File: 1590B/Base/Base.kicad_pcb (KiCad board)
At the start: 2 copper layers, 54 x 106 mm, 44 parts, among them J101 Barrel_Jack_Switch, J102 AudioJack3_SwitchTR, J103 AudioJack3_SwitchTR, J201 Conn_02x04_Odd_Even, Q101 PMV250, Q102 BC846, Q103 BC846, Q201 LS844, Q301 DMC3071LVT, Q302 DMC3071LVT, SW101 SW_Push_SPDT, U101 Daisy Seed

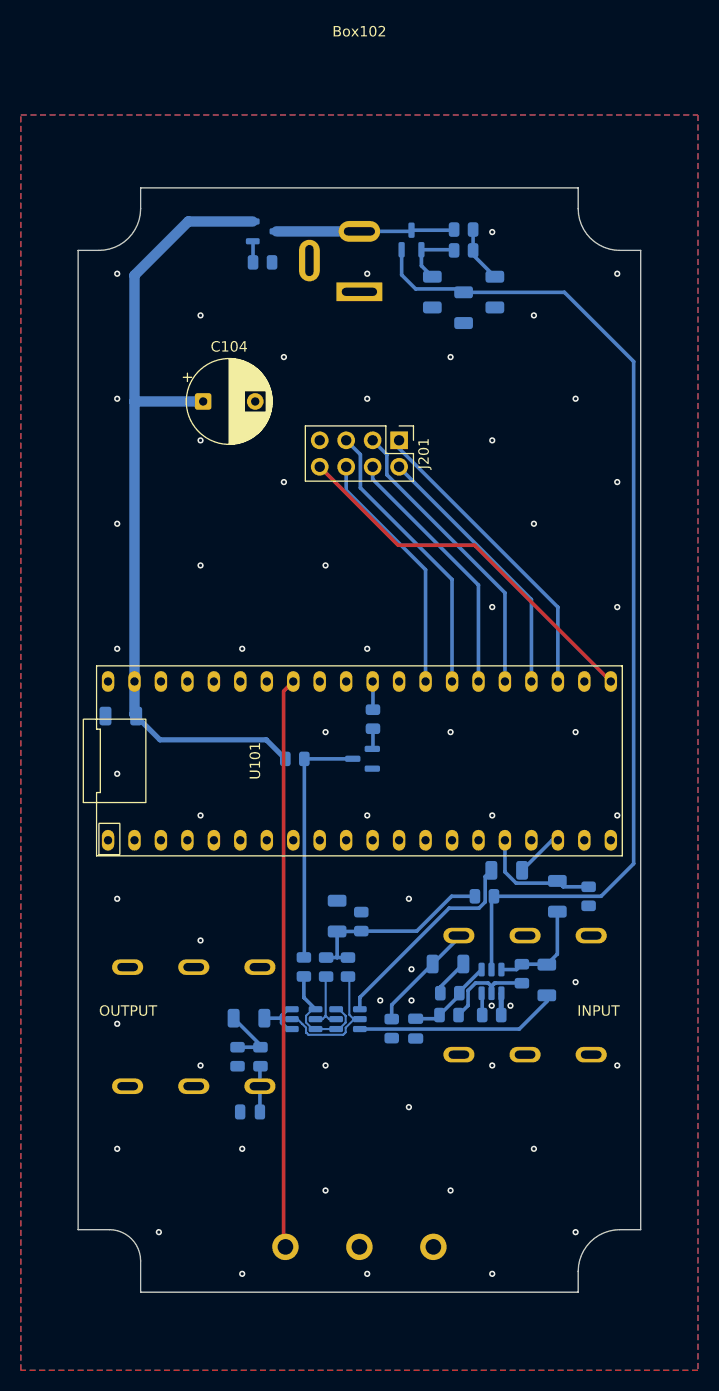
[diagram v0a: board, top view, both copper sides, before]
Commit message: Update 1590B board for sanity
I had entirely forgotten the activity LED, which was really annoying
when testing.

Also, while the transistor follower / capacitor multiplier on the analog
power supply was interesting for some low frequency power supply ripple
removal in simulation, it doesn't actually make any sense with any
modern power supply, so just do a regular RC filter for high
frequencies, which is what actually matters.

Together with the fixed potentiometer board, I think this should now
work nicely.

Famous last words.

Signed-off-by: Linus Torvalds <torvalds@linux-foundation.org>
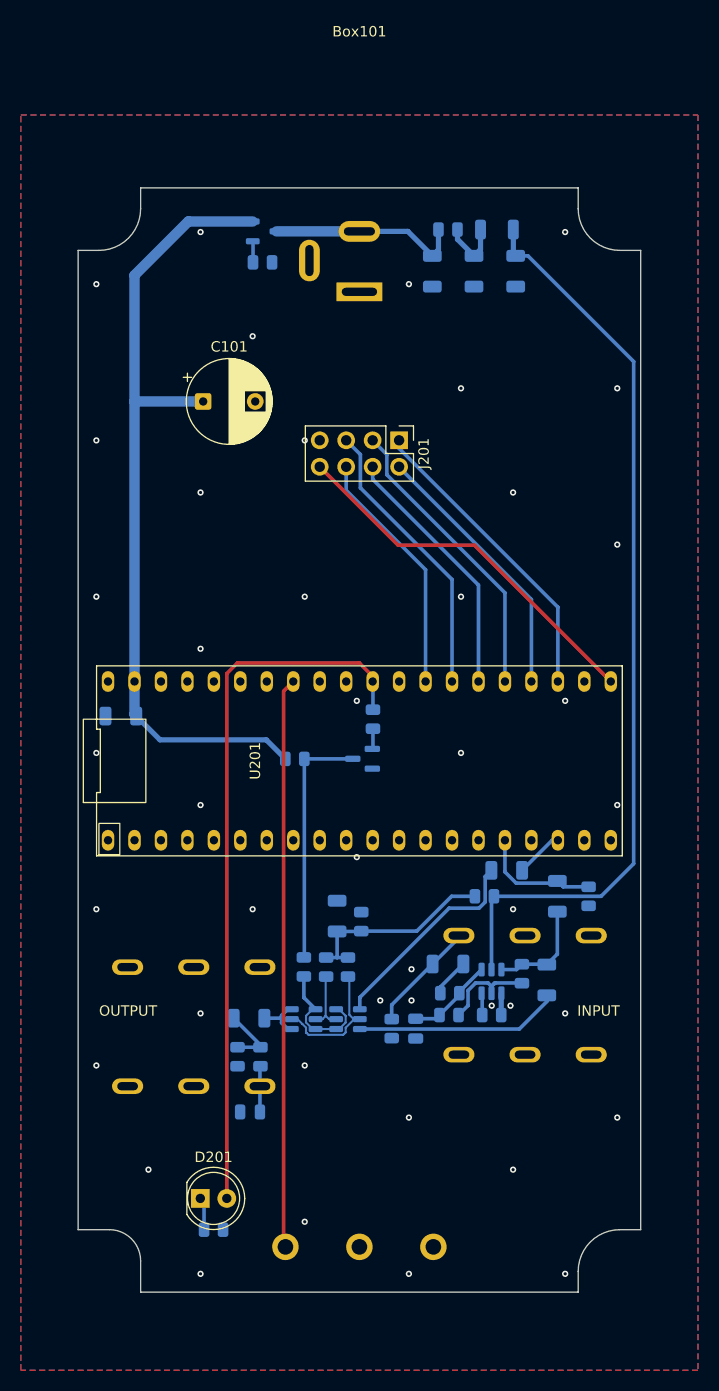
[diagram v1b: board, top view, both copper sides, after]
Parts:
- removed the C101 at (113.0, 57.0)
- removed Q102: BC846, Package_TO_SOT_SMD:SOT-23
- removed R106, R107: 2k2, Resistor_SMD:R_0805_2012Metric
- added C104: 1uF, Capacitor_SMD:C_1206_3216Metric, B.Cu at (115.0, 55.0)
- added D201: LED, LED_THT:LED_D5.0mm, F.Cu at (84.7, 144.0)
- added FB101: FerriteBead, Inductor_SMD:L_1206_3216Metric, B.Cu at (113.2, 51.0)
- added R102: 100R, Resistor_SMD:R_0805_2012Metric, B.Cu at (108.5, 51.0)
- added R209: 1k, Resistor_SMD:R_0805_2012Metric, B.Cu at (86.0, 147.0)
- moved C102 4.61 mm to (107.0, 55.0), turned to 90 degrees
- moved C103 4.47 mm to (111.0, 55.0), turned to 90 degrees
- renumbered Box102 to Box101, C104 to C101, C204 to C201, C201 to C204, Q103 to Q202, R102 to R207, R103 to R208, SW101 to SW201, U101 to U201
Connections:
- C102 pad 1: +VA -> GND
- C102 pad 2: GND -> PWRIN
- C103 pad 1: Net-(Q102-B) -> GND
- C103 pad 2: GND -> Net-(C103-Pad2)
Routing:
- net ON_OFF: track 2.72 -> 68.6 mm
- net +VA: track 98.7 -> 88.2 mm
- net Net-(Q102-B): track 6.19 -> 0.00 mm
- net Net-(C103-Pad2): track 0.00 -> 5.97 mm
- net Net-(C101-Pad1): track 5.39 -> 0.00 mm
- net Net-(D201-K): track 0.00 -> 3.15 mm
- net PWRIN: track 17.1 -> 18.7 mm
- net GND: vias 57 -> 43
